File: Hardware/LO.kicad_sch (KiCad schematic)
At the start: 2 parts

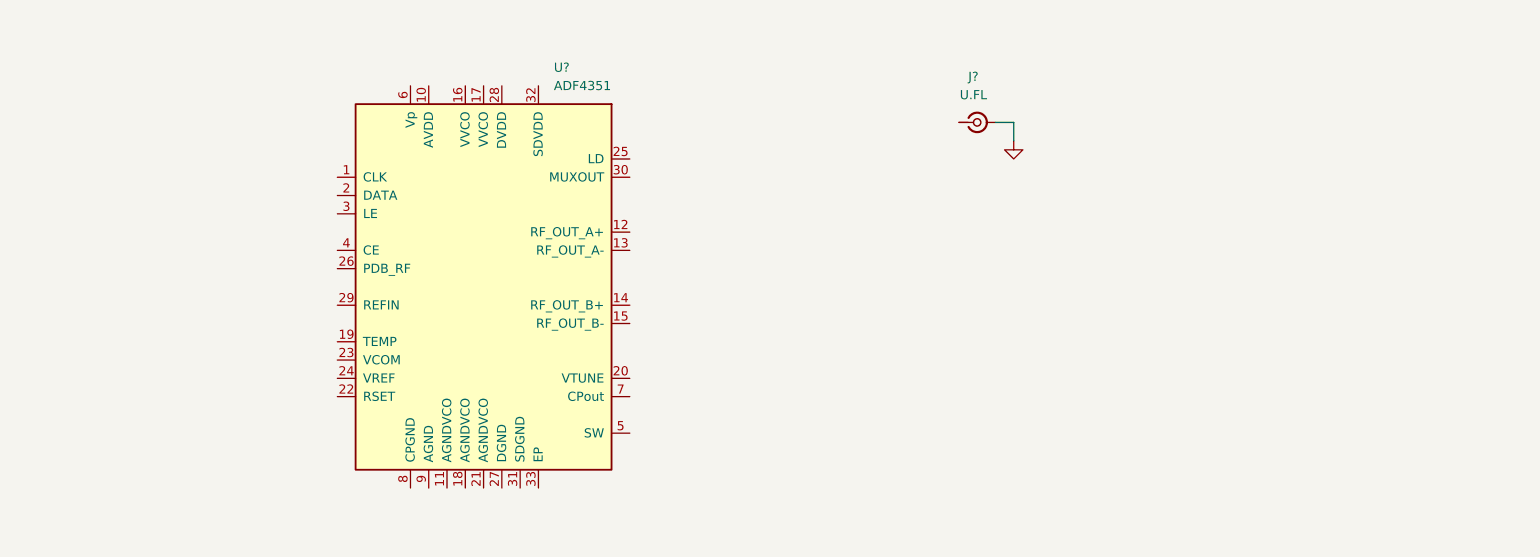
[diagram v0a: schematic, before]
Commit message: LO Loop Filter + Sims
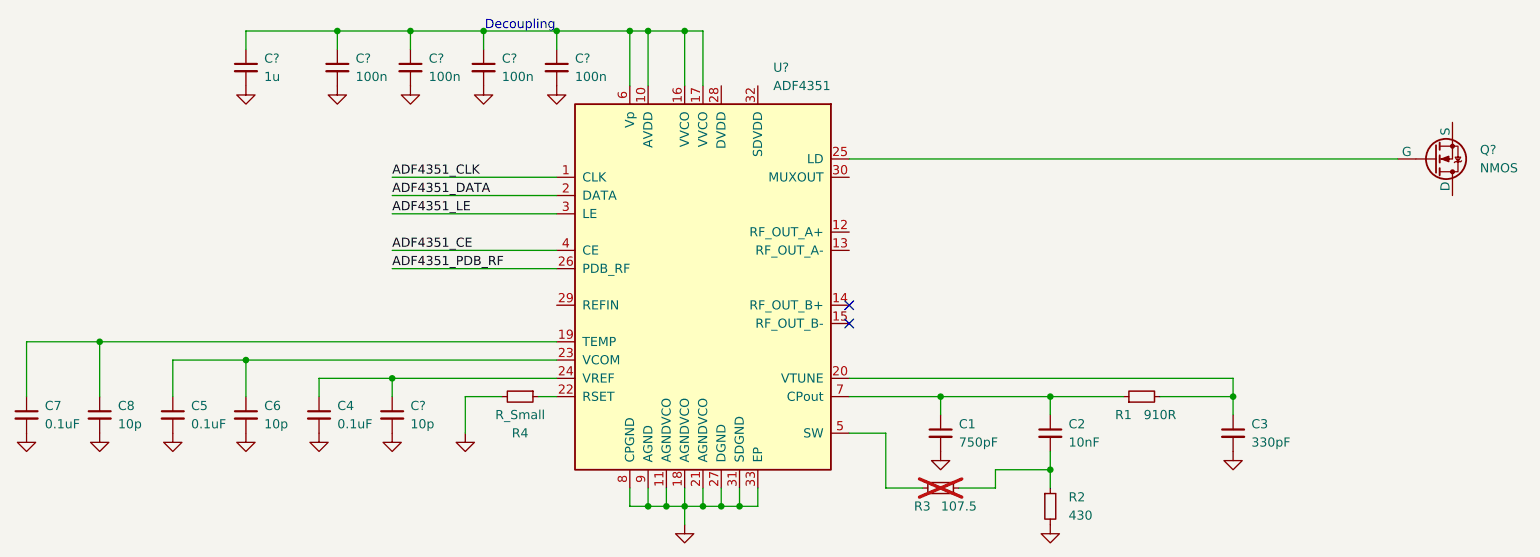
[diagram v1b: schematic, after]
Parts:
- removed J?: U.FL, symbol Connector:Conn_Coaxial_Small
- added C1: 750pF, symbol Device:C_Small
- added C2: 10nF, symbol Device:C_Small
- added C3: 330pF, symbol Device:C_Small
- added C4, C5, C7: 0.1uF, symbol Device:C_Small
- added C6, C8, C?: 10p, symbol Device:C_Small
- added C? (x4): 100n, symbol Device:C_Small
- added C?: 1u, symbol Device:C_Small
- added Q?: NMOS, symbol Simulation_SPICE:NMOS
- added R1: 910R, symbol Device:R_Small
- added R2: 430, symbol Device:R_Small
- added R3: 107.5, symbol Device:R_Small
- added R4: R_Small, symbol Device:R_Small
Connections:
- net GND: now also U?.11 (AGNDVCO), U?.18 (AGNDVCO), U?.21 (AGNDVCO), U?.27 (DGND), U?.31 (SDGND), U?.33 (EP), U?.8 (CPGND), U?.9 (AGND), C1.2, C3.2, C4.2, C5.2, C6.2, C7.2, C8.2, C?.2, C?.2, C?.2, C?.2, C?.2, C?.2, R2.2, R4.2
- net ADF4351_CLK: now reaches U?.1 (CLK)
- net at U?.10 (AVDD): now also U?.16 (VVCO), U?.17 (VVCO), U?.6 (Vp), C?.1, C?.1, C?.1, C?.1, C?.1
- net at U?.19 (TEMP): now also C7.1, C8.1
- net ADF4351_DATA: now reaches U?.2 (DATA)
- net at U?.20 (VTUNE): now also C3.1, R1.2
- net at U?.22 (RSET): now also R4.1
- net at U?.23 (VCOM): now also C5.1, C6.1
- net at U?.24 (VREF): now also C4.1, C?.1
- net at U?.25 (LD): now also Q?.2 (G)
- net ADF4351_PDB_RF: now reaches U?.26 (PDB_RF)
- net ADF4351_LE: now reaches U?.3 (LE)
- net ADF4351_CE: now reaches U?.4 (CE)
- net at U?.5 (SW): now also R3.2
- net at U?.7 (CPout): now also C1.1, C2.1, R1.1
- new net: C2.2, R2.1, R3.1
- no-connect marks 0 -> 2
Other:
- note added: "Decoupling"
- moved on the sheet: U?
